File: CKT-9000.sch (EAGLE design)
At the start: 7 parts, among them J1 PWR IN, J2 PWR OUT, J3 PI USB, J4 RX USB

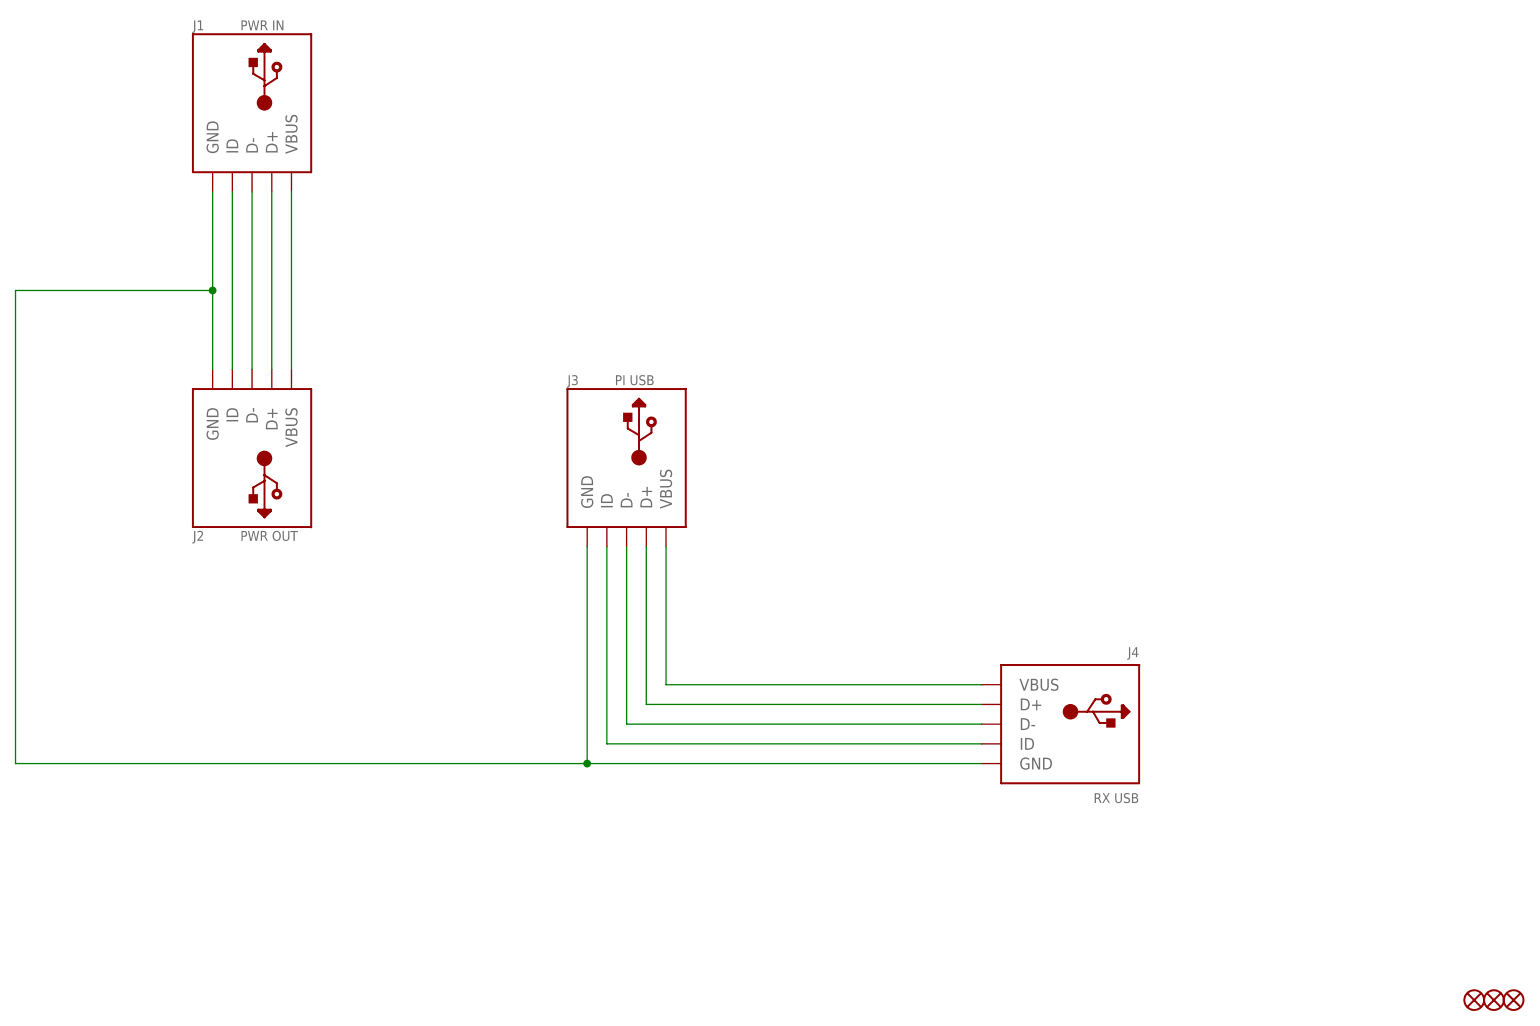
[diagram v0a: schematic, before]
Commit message: Adds a MOSFET and gate bias resistor to the board. The ID pin of the PWR IN usb connector is utilized as the signal to turn the MOSFET on/off.
Eagle Cad updated to v 9.5.1
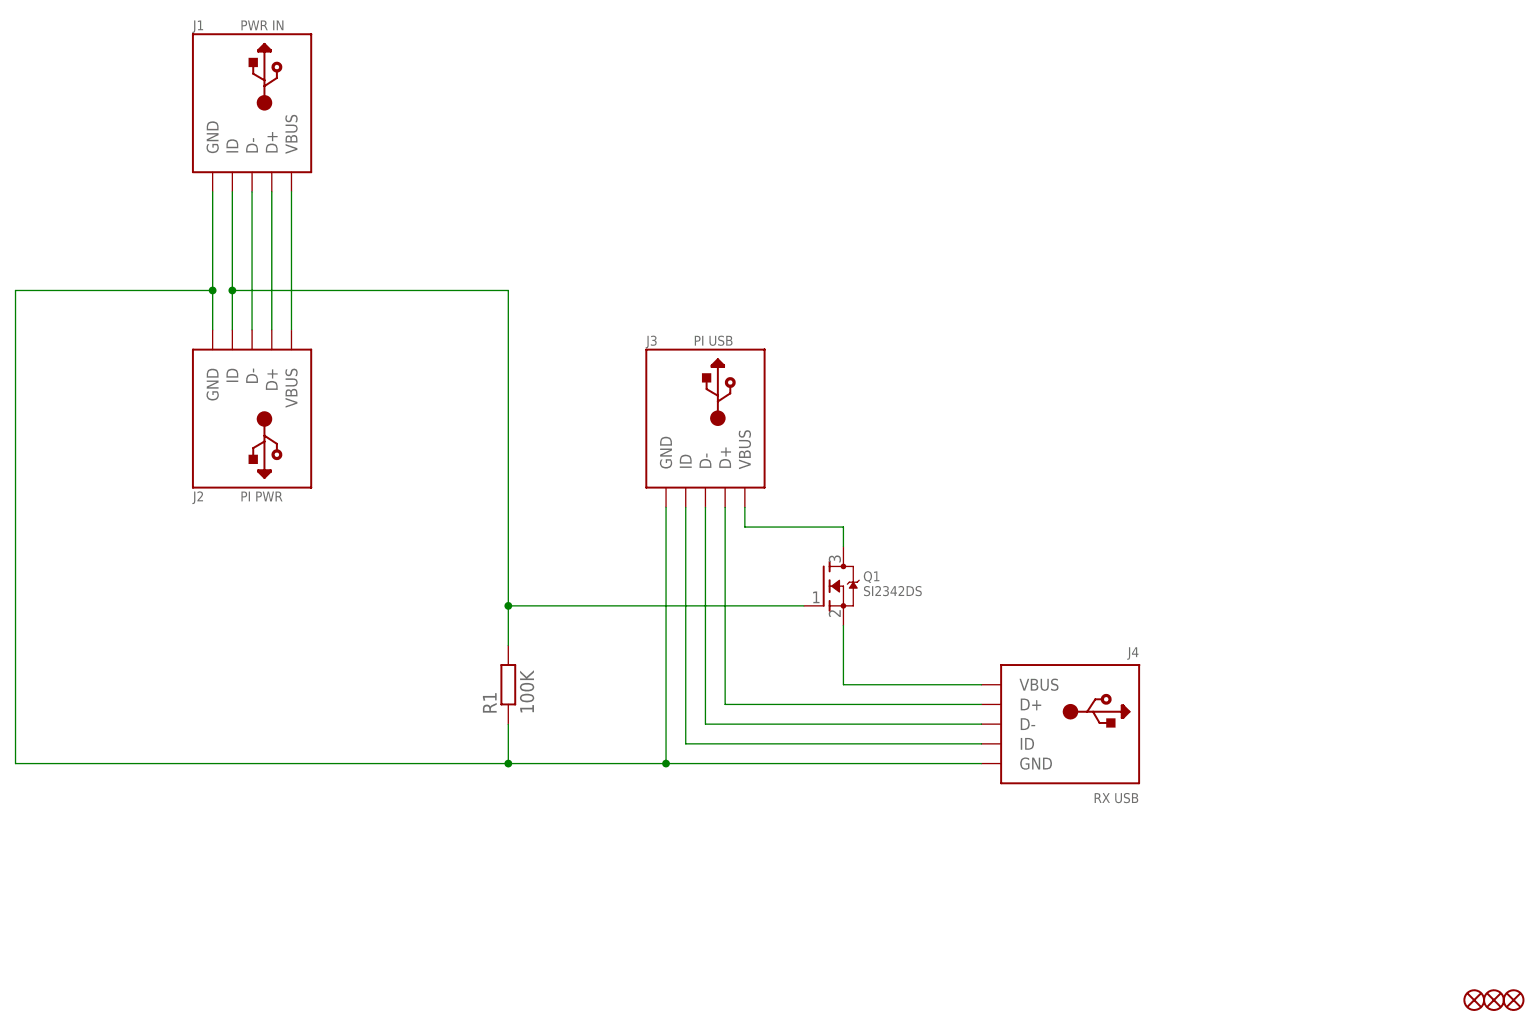
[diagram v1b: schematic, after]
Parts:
- added Q1: SI2342DS, brunnertech:MOSFET-NREFLOW
- added R1: 100K, brunnertech:R-EU_R0805
- J2: value PWR OUT -> PI PWR
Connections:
- removed net ID$1: J1.ID, J2.ID
- removed net VBUS$2: J3.VBUS, J4.VBUS
- new net N$1: J3.VBUS, Q1.D
- new net N$2: J4.VBUS, Q1.S
- new net N$3: J1.ID, J2.ID, Q1.G, R1.2
- net GND: now also R1.1
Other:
- moved on the sheet: J2, J3

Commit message: Adds a second MOSFET (p-channel) along with an additional resistor to make the circuit actually do what it is supposed to. I obviously didn't think about the prior design very thoroughly! Here's the circuit I'm using to shoot for the correct behavior (with different FET's though): https://electronics.stackexchange.com/a/353222.  I also updated Eagle to the next minor release (9.5.2).
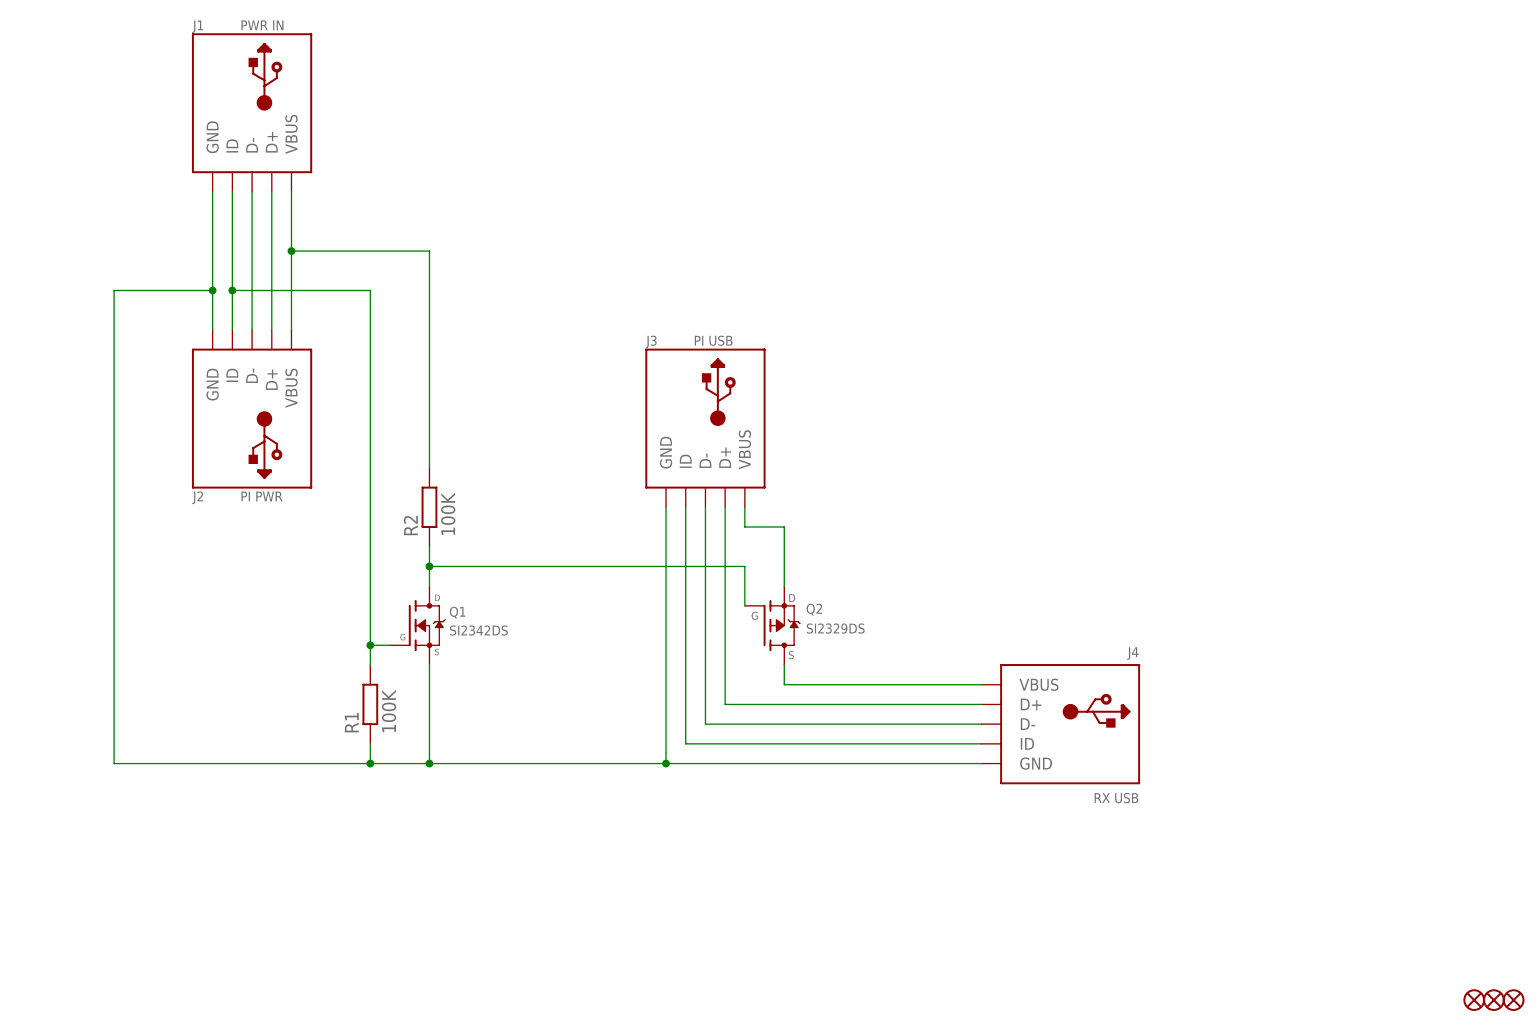
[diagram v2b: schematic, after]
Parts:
- added Q2: SI2329DS, brunnertech:MOSFET-PSOT23
- added R2: 100K, brunnertech:R-EU_R0805
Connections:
- new net N$4: J4.VBUS, Q2.D
- net GND: now also Q1.S
- net N$1: now also Q2.G, R2.1; no longer J3.VBUS
- net N$2: now also J3.VBUS, Q2.S; no longer J4.VBUS, Q1.S
- net VBUS$1: now also R2.2
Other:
- moved on the sheet: Q1, R1
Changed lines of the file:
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@@
 <?xml version="1.0" encoding="utf-8"?>
 <!DOCTYPE eagle SYSTEM "eagle.dtd">
-<eagle version="9.5.1">
+<eagle version="9.5.2">
 <drawing>
 <settings>
@@
 <attributes>
 <attribute name="DWG_NUMBER" value="CKT-9000"/>
-<attribute name="REV" value="A"/>
+<attribute name="REV" value="B"/>
 <attribute name="TITLE" value="PIMTECTOR USB MANIFOLD"/>
 </attributes>
@@
 <part name="Q1" library="brunnertech" deviceset="MOSFET-N" device="REFLOW" value="SI2342DS"/>
 <part name="R1" library="brunnertech" deviceset="R-EU_" device="R0805" package3d_urn="urn:adsk.eagle:package:23553/2" value="100K"/>
+<part name="Q2" library="brunnertech" deviceset="MOSFET-P" device="SOT23" value="SI2329DS"/>
+<part name="R2" library="brunnertech" deviceset="R-EU_" device="R0805" package3d_urn="urn:adsk.eagle:package:23553/2" value="100K"/>
 </parts>
 <sheets>
@@
 <attribute name="REV" x="264.16" y="7.62" size="2.54" layer="94"/>
 </instance>
-<instance part="Q1" gate="G$1" x="170.18" y="101.6" smashed="yes">
-<attribute name="NAME" x="175.26" y="102.235" size="1.27" layer="95"/>
-<attribute name="VALUE" x="175.26" y="100.33" size="1.27" layer="96"/>
-</instance>
-<instance part="R1" gate="G$1" x="129.54" y="88.9" smashed="yes" rot="R90">
-<attribute name="NAME" x="128.0414" y="85.09" size="1.778" layer="95" rot="R90"/>
-<attribute name="VALUE" x="132.842" y="85.09" size="1.778" layer="96" rot="R90"/>
+<instance part="Q1" gate="G$1" x="119.38" y="96.52" smashed="yes">
+<attribute name="NAME" x="121.92" y="97.663" size="1.27" layer="95"/>
+<attribute name="VALUE" x="121.92" y="95.25" size="1.27" layer="96"/>
+</instance>
+<instance part="R1" gate="G$1" x="111.76" y="86.36" smashed="yes" rot="R90">
+<attribute name="NAME" x="110.2614" y="82.55" size="1.778" layer="95" rot="R90"/>
+<attribute name="VALUE" x="115.062" y="82.55" size="1.778" layer="96" rot="R90"/>
+</instance>
+<instance part="Q2" gate="G$1" x="165.1" y="96.52" smashed="yes">
+<attribute name="VALUE" x="167.894" y="95.504" size="1.27" layer="96"/>
+<attribute name="NAME" x="167.894" y="98.044" size="1.27" layer="95"/>
+</instance>
+<instance part="R2" gate="G$1" x="119.38" y="111.76" smashed="yes" rot="R90">
+<attribute name="NAME" x="117.8814" y="107.95" size="1.778" layer="95" rot="R90"/>
+<attribute name="VALUE" x="122.682" y="107.95" size="1.778" layer="96" rot="R90"/>
 </instance>
 </instances>
@@
 <wire x1="91.44" y1="152.4" x2="91.44" y2="139.7" width="0.1524" layer="91"/>
 <wire x1="91.44" y1="139.7" x2="91.44" y2="134.62" width="0.1524" layer="91"/>
-<wire x1="91.44" y1="139.7" x2="66.04" y2="139.7" width="0.1524" layer="91"/>
+<wire x1="91.44" y1="139.7" x2="78.74" y2="139.7" width="0.1524" layer="91"/>
 <junction x="91.44" y="139.7"/>
 <pinref part="J3" gate="G$1" pin="GND"/>
+<wire x1="149.86" y1="111.76" x2="149.86" y2="78.74" width="0.1524" layer="91"/>
+<wire x1="78.74" y1="139.7" x2="78.74" y2="78.74" width="0.1524" layer="91"/>
+<wire x1="78.74" y1="78.74" x2="111.76" y2="78.74" width="0.1524" layer="91"/>
+<wire x1="111.76" y1="78.74" x2="119.38" y2="78.74" width="0.1524" layer="91"/>
+<wire x1="119.38" y1="78.74" x2="149.86" y2="78.74" width="0.1524" layer="91"/>
+<wire x1="111.76" y1="81.28" x2="111.76" y2="78.74" width="0.1524" layer="91"/>
+<junction x="111.76" y="78.74"/>
+<pinref part="R1" gate="G$1" pin="1"/>
+<pinref part="Q1" gate="G$1" pin="S"/>
+<wire x1="119.38" y1="91.44" x2="119.38" y2="78.74" width="0.1524" layer="91"/>
+<junction x="119.38" y="78.74"/>
 <pinref part="J4" gate="G$1" pin="GND"/>
-<wire x1="149.86" y1="111.76" x2="149.86" y2="78.74" width="0.1524" layer="91"/>
-<wire x1="149.86" y1="78.74" x2="190.5" y2="78.74" width="0.1524" layer="91"/>
-<wire x1="66.04" y1="139.7" x2="66.04" y2="78.74" width="0.1524" layer="91"/>
-<wire x1="66.04" y1="78.74" x2="129.54" y2="78.74" width="0.1524" layer="91"/>
+<wire x1="190.5" y1="78.74" x2="149.86" y2="78.74" width="0.1524" layer="91"/>
 <junction x="149.86" y="78.74"/>
-<wire x1="129.54" y1="78.74" x2="149.86" y2="78.74" width="0.1524" layer="91"/>
-<wire x1="129.54" y1="83.82" x2="129.54" y2="78.74" width="0.1524" layer="91"/>
-<junction x="129.54" y="78.74"/>
-<pinref part="R1" gate="G$1" pin="1"/>
 </segment>
 </net>
@@
 <pinref part="J1" gate="G$1" pin="VBUS"/>
 <pinref part="J2" gate="G$1" pin="VBUS"/>
-<wire x1="101.6" y1="152.4" x2="101.6" y2="134.62" width="0.1524" layer="91"/>
+<wire x1="101.6" y1="152.4" x2="101.6" y2="144.78" width="0.1524" layer="91"/>
+<pinref part="R2" gate="G$1" pin="2"/>
+<wire x1="101.6" y1="144.78" x2="101.6" y2="134.62" width="0.1524" layer="91"/>
+<wire x1="119.38" y1="116.84" x2="119.38" y2="144.78" width="0.1524" layer="91"/>
+<wire x1="119.38" y1="144.78" x2="101.6" y2="144.78" width="0.1524" layer="91"/>
+<junction x="101.6" y="144.78"/>
 </segment>
 </net>
@@
 </segment>
 </net>
-<net name="N$1" class="0">
-<segment>
-<pinref part="J3" gate="G$1" pin="VBUS"/>
-<wire x1="160.02" y1="111.76" x2="160.02" y2="109.22" width="0.1524" layer="91"/>
-<wire x1="160.02" y1="109.22" x2="172.72" y2="109.22" width="0.1524" layer="91"/>
-<pinref part="Q1" gate="G$1" pin="D"/>
-<wire x1="172.72" y1="109.22" x2="172.72" y2="106.68" width="0.1524" layer="91"/>
-</segment>
-</net>
-<net name="N$2" class="0">
-<segment>
-<pinref part="Q1" gate="G$1" pin="S"/>
-<wire x1="172.72" y1="96.52" x2="172.72" y2="88.9" width="0.1524" layer="91"/>
-<pinref part="J4" gate="G$1" pin="VBUS"/>
-<wire x1="172.72" y1="88.9" x2="190.5" y2="88.9" width="0.1524" layer="91"/>
-</segment>
-</net>
 <net name="N$3" class="0">
 <segment>
@@
 <wire x1="93.98" y1="152.4" x2="93.98" y2="139.7" width="0.1524" layer="91"/>
 <wire x1="93.98" y1="139.7" x2="93.98" y2="134.62" width="0.1524" layer="91"/>
-<wire x1="93.98" y1="139.7" x2="129.54" y2="139.7" width="0.1524" layer="91"/>
+<wire x1="93.98" y1="139.7" x2="111.76" y2="139.7" width="0.1524" layer="91"/>
 <junction x="93.98" y="139.7"/>
+<pinref part="R1" gate="G$1" pin="2"/>
+<wire x1="111.76" y1="91.44" x2="111.76" y2="93.98" width="0.1524" layer="91"/>
 <pinref part="Q1" gate="G$1" pin="G"/>
-<wire x1="167.64" y1="99.06" x2="129.54" y2="99.06" width="0.1524" layer="91"/>
-<wire x1="129.54" y1="99.06" x2="129.54" y2="93.98" width="0.1524" layer="91"/>
-<wire x1="129.54" y1="139.7" x2="129.54" y2="99.06" width="0.1524" layer="91"/>
-<junction x="129.54" y="99.06"/>
-<pinref part="R1" gate="G$1" pin="2"/>
-</segment>
-</net>
+<wire x1="111.76" y1="93.98" x2="111.76" y2="139.7" width="0.1524" layer="91"/>
+<wire x1="114.3" y1="93.98" x2="111.76" y2="93.98" width="0.1524" layer="91"/>
+<junction x="111.76" y="93.98"/>
+</segment>
+</net>
+<net name="N$1" class="0">
+<segment>
+<pinref part="R2" gate="G$1" pin="1"/>
+<pinref part="Q1" gate="G$1" pin="D"/>
+<wire x1="119.38" y1="106.68" x2="119.38" y2="104.14" width="0.1524" layer="91"/>
+<pinref part="Q2" gate="G$1" pin="G"/>
+<wire x1="119.38" y1="104.14" x2="119.38" y2="101.6" width="0.1524" layer="91"/>
+<wire x1="119.38" y1="104.14" x2="160.02" y2="104.14" width="0.1524" layer="91"/>
+<wire x1="160.02" y1="104.14" x2="160.02" y2="99.06" width="0.1524" layer="91"/>
+<junction x="119.38" y="104.14"/>
+</segment>
+</net>
+<net name="N$2" class="0">
+<segment>
+<pinref part="J3" gate="G$1" pin="VBUS"/>
+<wire x1="160.02" y1="111.76" x2="160.02" y2="109.22" width="0.1524" layer="91"/>
+<wire x1="160.02" y1="109.22" x2="165.1" y2="109.22" width="0.1524" layer="91"/>
+<pinref part="Q2" gate="G$1" pin="S"/>
+<wire x1="165.1" y1="109.22" x2="165.1" y2="101.6" width="0.1524" layer="91"/>
+</segment>
+</net>
+<net name="N$4" class="0">
+<segment>
+<pinref part="Q2" gate="G$1" pin="D"/>
+<wire x1="165.1" y1="91.44" x2="165.1" y2="88.9" width="0.1524" layer="91"/>
+<pinref part="J4" gate="G$1" pin="VBUS"/>
+<wire x1="165.1" y1="88.9" x2="190.5" y2="88.9" width="0.1524" layer="91"/>
+</segment>
+</net>
